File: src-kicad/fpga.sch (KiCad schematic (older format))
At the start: 28 parts, among them U1 iCE40HX1K-TQ144, U2 N25Q032A

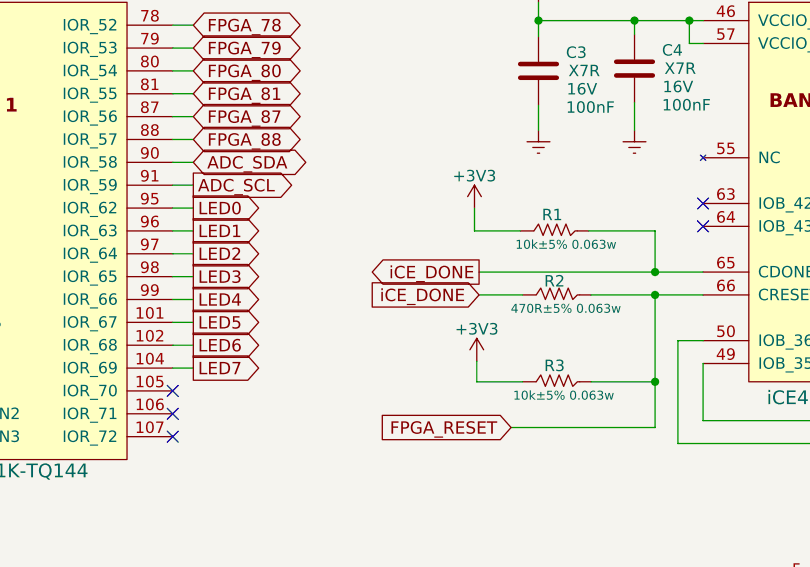
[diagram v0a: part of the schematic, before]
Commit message: Kicad migration: schematic initial version migrated. 0 errors in electrical rule check
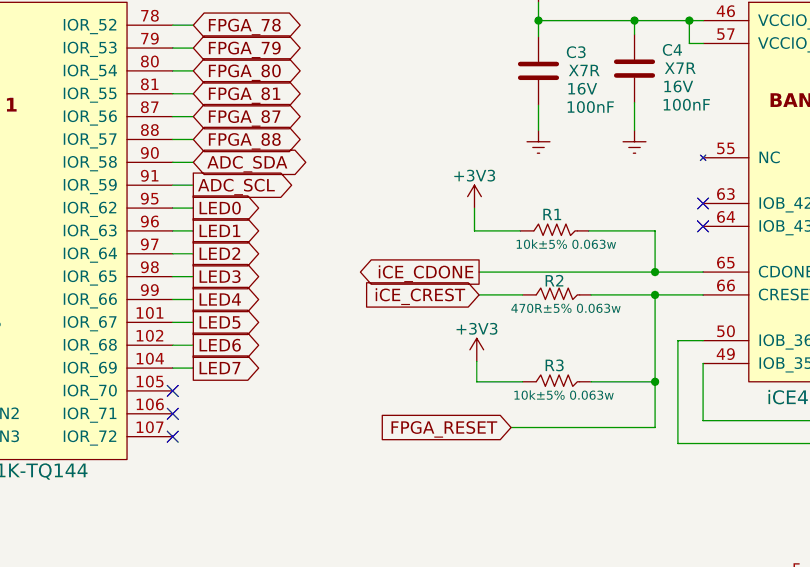
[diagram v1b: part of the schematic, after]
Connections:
- net iCE_DONE renamed iCE_CDONE
- net iCE_CDONE: no longer R2.2
- new net iCE_CREST: R2.2
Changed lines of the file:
@@
 NoConn ~ 10050 2180
 Text GLabel 7670 1980 0    54   Output ~ 0
-iCE_DONE
+iCE_CDONE
 Text GLabel 7670 2080 0    54   Input ~ 0
-iCE_DONE
+iCE_CREST
 $Comp
 L R R2

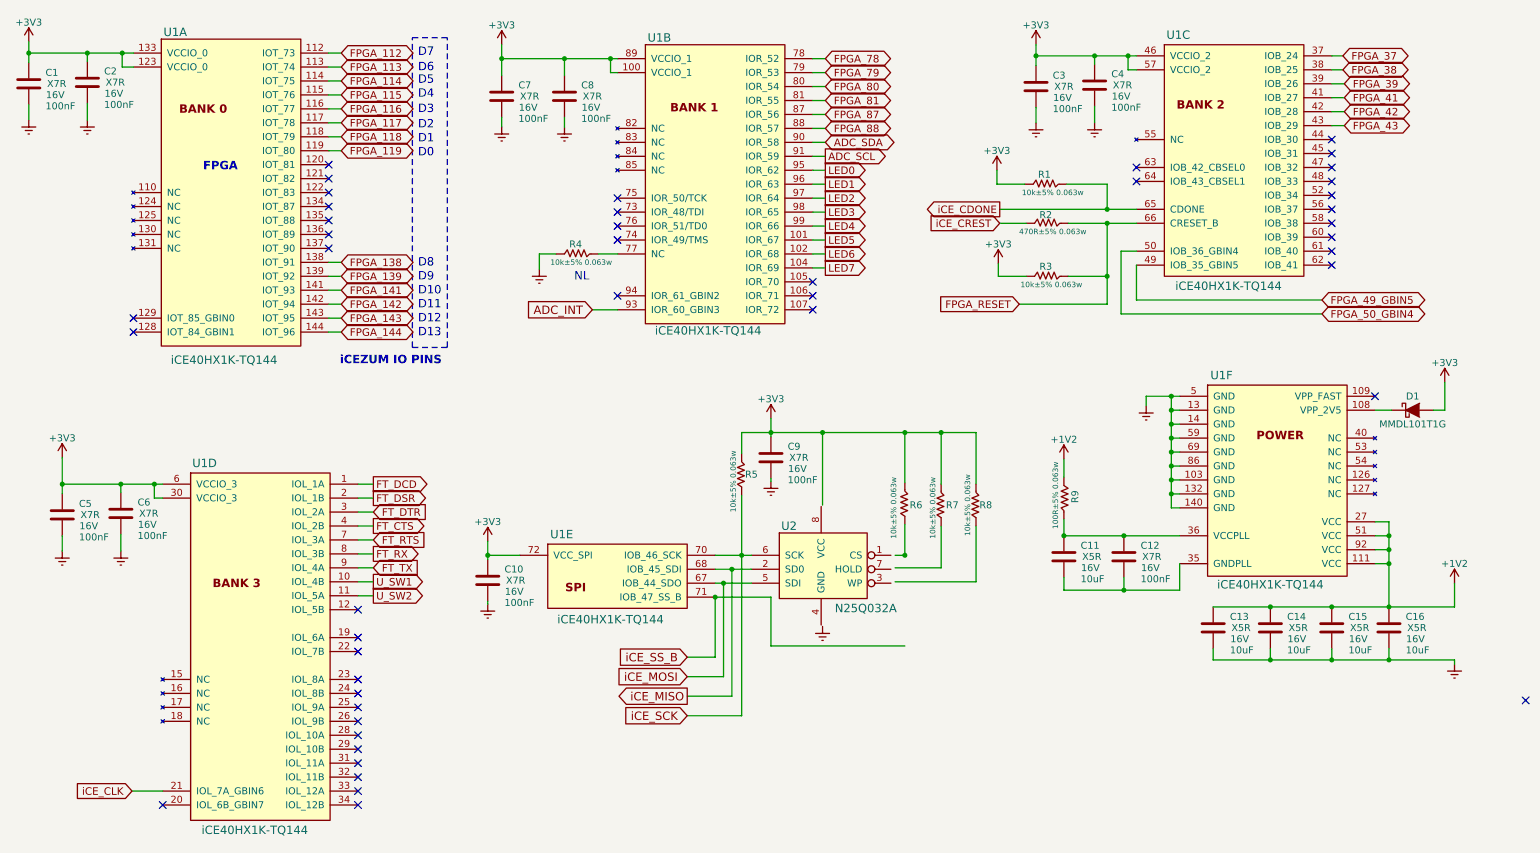
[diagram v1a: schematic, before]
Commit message: Kicad schematic: fpga sheet: aligned to 50mils grid
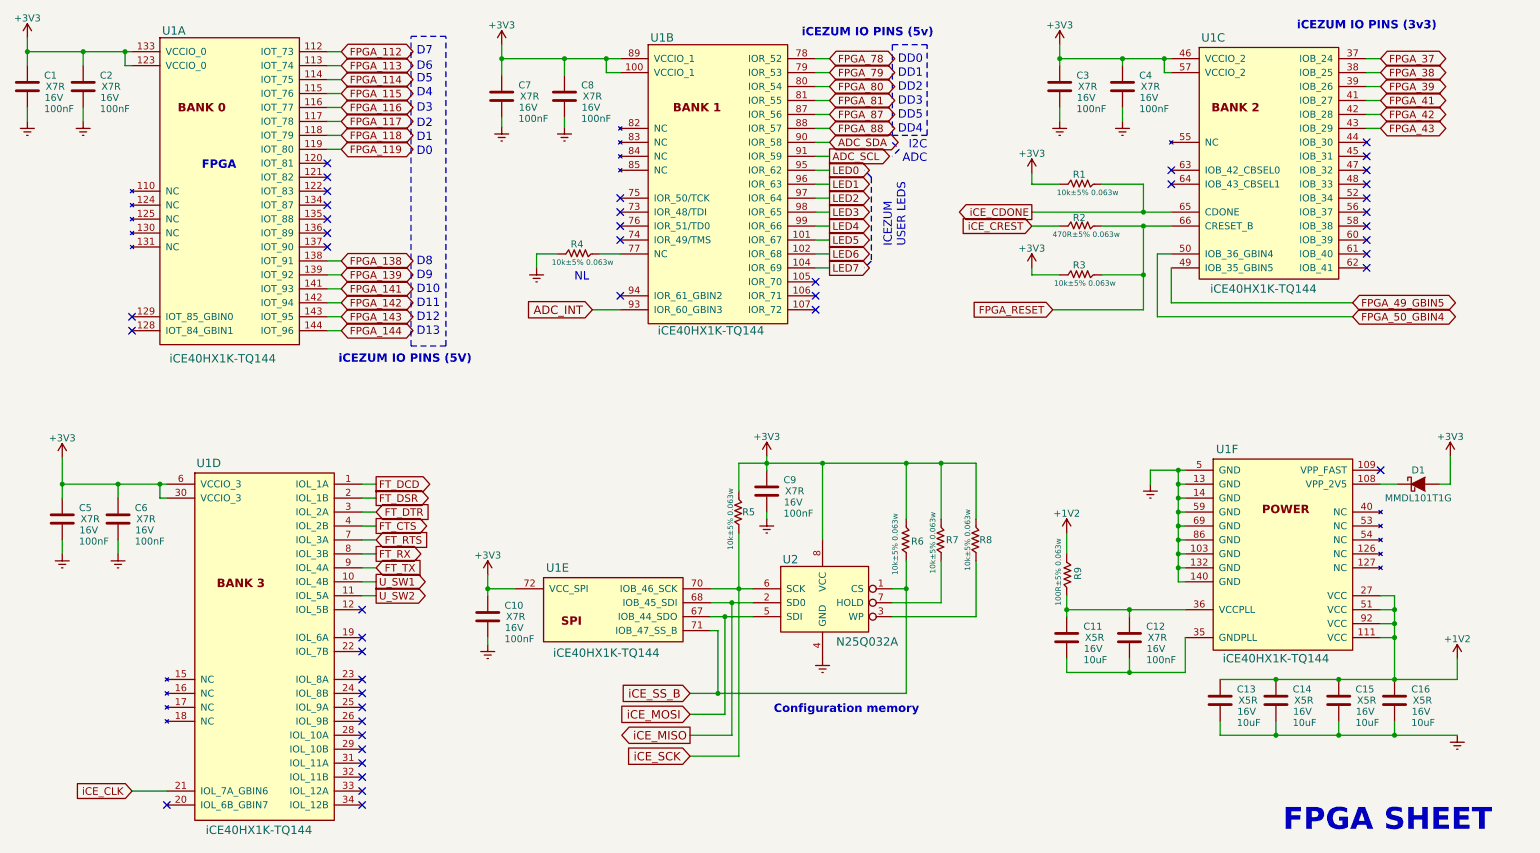
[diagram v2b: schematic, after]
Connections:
- net +3V3: now also U2.8 (VCC)
- net FPGA_RESET: no longer R2.1, U1.66 (CRESET_B)
- net GNDREF: now also U2.4 (GND)
- net iCE_SS_B: now also R6.2, U2.1 (CS)
- net at U2.3 (WP): now also R8.2
- net at U2.7 (HOLD): now also R7.2
- new net: R2.1, U1.66 (CRESET_B)
- no-connect marks 45 -> 44
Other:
- note added: "Configuration memory"
- note added: "DD0"
- note added: "DD1"
- note added: "DD2"
- note added: "DD3"
- note added: "DD4"
- note added: "DD5"
- note added: "FPGA SHEET"
- note added: "I2C\nADC"
- note added: "ICEZUM \nUSER LEDS"
- note added: "iCEZUM IO PINS (3v3)"
- note added: "iCEZUM IO PINS (5V)"
- note added: "iCEZUM IO PINS (5v)"
- note removed: "iCEZUM IO PINS"
- moved on the sheet: C1, C10, C11, C12, C13, C14, C15, C16, C2, C3, C4, C5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

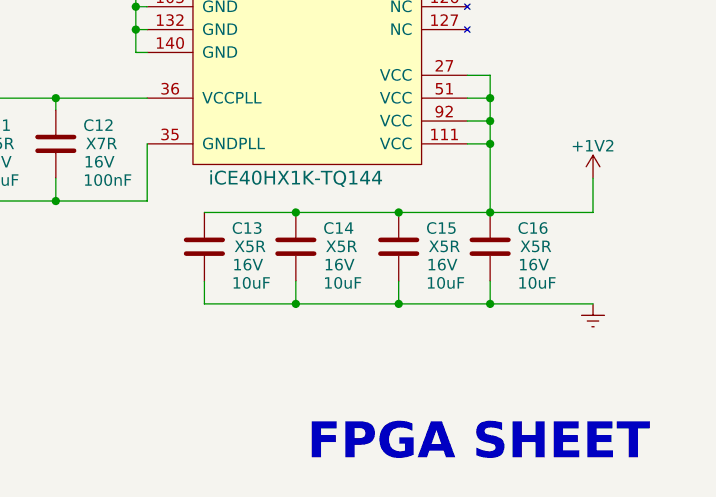
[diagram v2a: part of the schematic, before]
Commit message: Kicad schematic: added fpgawars logo and CC-BY-SA to all the sheets
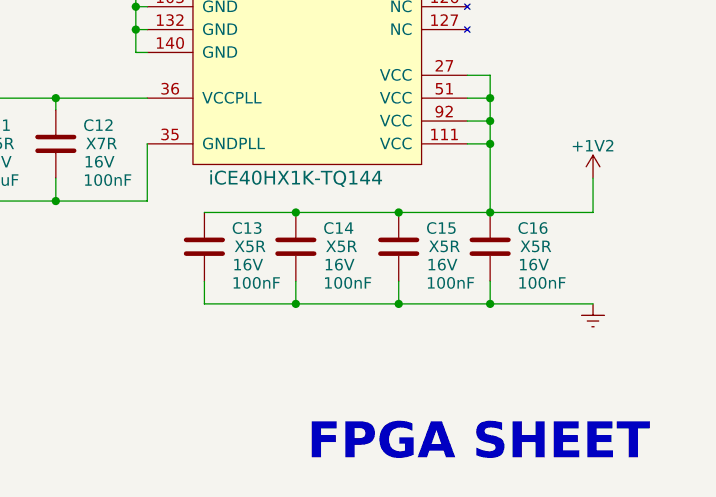
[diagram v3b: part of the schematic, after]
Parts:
- C13, C14, C15, C16: value 10uF -> 100nF
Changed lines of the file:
@@
 Comp "FPGAwars"
 Comment1 "Migration to kicad:  Juan Gonzalez (Obijuan)"
-Comment2 "Author: Eladio Delagado Mingorance"
+Comment2 "Author:  Eladio Delagado Mingorance"
 Comment3 "License: Creative commons Attribution ShareAlike "
 Comment4 ""
@@
 P 9250 5500
 F 0 "C13" H 9370 5580 50  0000 L CNN
-F 1 "10uF" H 9370 5340 50  0000 L CNN
+F 1 "100nF" H 9370 5340 50  0000 L CNN
 F 2 "" H 9288 5350 50  0000 C CNN
 F 3 "" H 9250 5500 50  0000 C CNN
@@
 P 9650 5500
 F 0 "C14" H 9770 5580 50  0000 L CNN
-F 1 "10uF" H 9770 5340 50  0000 L CNN
+F 1 "100nF" H 9770 5340 50  0000 L CNN
 F 2 "" H 9688 5350 50  0000 C CNN
 F 3 "" H 9650 5500 50  0000 C CNN
@@
 P 10100 5500
 F 0 "C15" H 10220 5580 50  0000 L CNN
-F 1 "10uF" H 10220 5340 50  0000 L CNN
+F 1 "100nF" H 10220 5340 50  0000 L CNN
 F 2 "" H 10138 5350 50  0000 C CNN
 F 3 "" H 10100 5500 50  0000 C CNN
@@
 P 10500 5500
 F 0 "C16" H 10620 5580 50  0000 L CNN
-F 1 "10uF" H 10620 5340 50  0000 L CNN
+F 1 "100nF" H 10620 5340 50  0000 L CNN
 F 2 "" H 10538 5350 50  0000 C CNN
 F 3 "" H 10500 5500 50  0000 C CNN

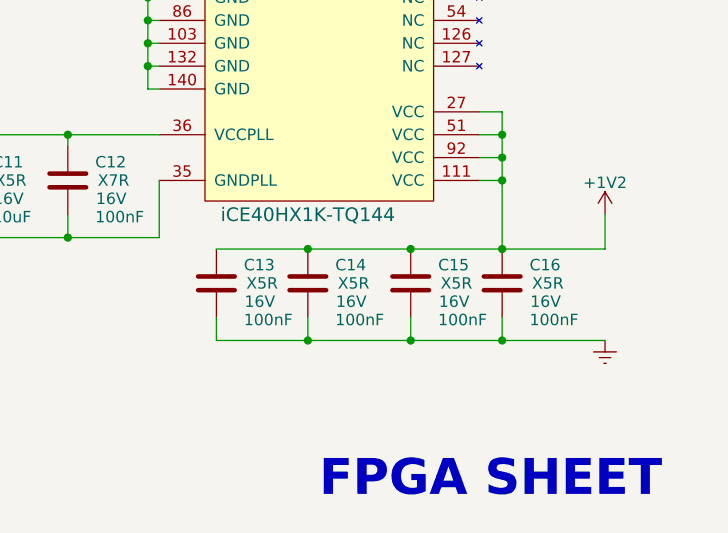
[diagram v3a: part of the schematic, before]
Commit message: Kicad schematic: FPGA sheet double checked
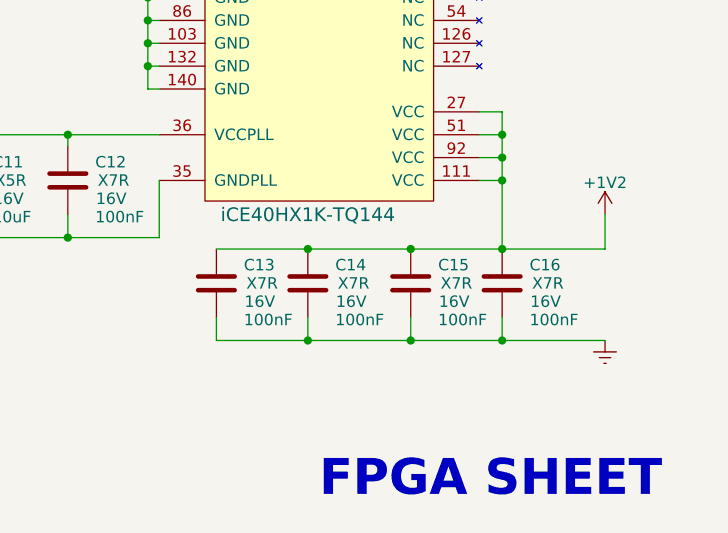
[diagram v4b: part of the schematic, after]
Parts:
- C13, C14, C15, C16: class X5R -> X7R
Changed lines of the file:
@@
 F 2 "" H 9288 5350 50  0000 C CNN
 F 3 "" H 9250 5500 50  0000 C CNN
-F 4 "X5R" H 9450 5500 50  0000 C CNN "class"
+F 4 "X7R" H 9450 5500 50  0000 C CNN "class"
 F 5 "16V" H 9440 5420 50  0000 C CNN "Voltage"
 	1    9250 5500
@@
 F 2 "" H 9688 5350 50  0000 C CNN
 F 3 "" H 9650 5500 50  0000 C CNN
-F 4 "X5R" H 9850 5500 50  0000 C CNN "class"
+F 4 "X7R" H 9850 5500 50  0000 C CNN "class"
 F 5 "16V" H 9840 5420 50  0000 C CNN "Voltage"
 	1    9650 5500
@@
 F 2 "" H 10138 5350 50  0000 C CNN
 F 3 "" H 10100 5500 50  0000 C CNN
-F 4 "X5R" H 10300 5500 50  0000 C CNN "class"
+F 4 "X7R" H 10300 5500 50  0000 C CNN "class"
 F 5 "16V" H 10290 5420 50  0000 C CNN "Voltage"
 	1    10100 5500
@@
 F 2 "" H 10538 5350 50  0000 C CNN
 F 3 "" H 10500 5500 50  0000 C CNN
-F 4 "X5R" H 10700 5500 50  0000 C CNN "class"
+F 4 "X7R" H 10700 5500 50  0000 C CNN "class"
 F 5 "16V" H 10690 5420 50  0000 C CNN "Voltage"
 	1    10500 5500
